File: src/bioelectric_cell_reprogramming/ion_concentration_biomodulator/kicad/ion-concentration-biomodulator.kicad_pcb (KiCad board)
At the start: 4 copper layers, 96 x 72 mm, 69 parts, among them J1 532610671, J10 39-53-2045, J11 Conn_01x14_Pin, J12 Conn_01x14_Pin, J13 39-53-2045, J14 39-53-2045, J15 Conn_ARM_SWD_TagConnect_TC2030, J16 IPL1-104-01-L-D-K, J17 Conn_01x02_Pin, J18 EJ508A, J19 USB_C_Receptacle_USB2.0_14P, J2 532610671, J20 6620XX11122_66200211122, J21 IPL1-102-01-L-S-K, J3 532610671, J4 532610671, J5 S4B-PH-SM4-TB, J6 Conn_01x02_Pin, J7 6620XX11122_66200211122, J8 39-53-2045, J9 IPL1-102-01-L-S-K, Q1 NDT3055L, Q2 NDT3055L, Q4 NDT3055L, Q5 NDT3055L, Q6 NDT3055L, SW1 SW_Push, U1 STM32F410CBTx, U2 LM1084-5.0, U3 LM1084-3.3, U4 USBLC6-2SC6, U5 DRV8873HPWPR

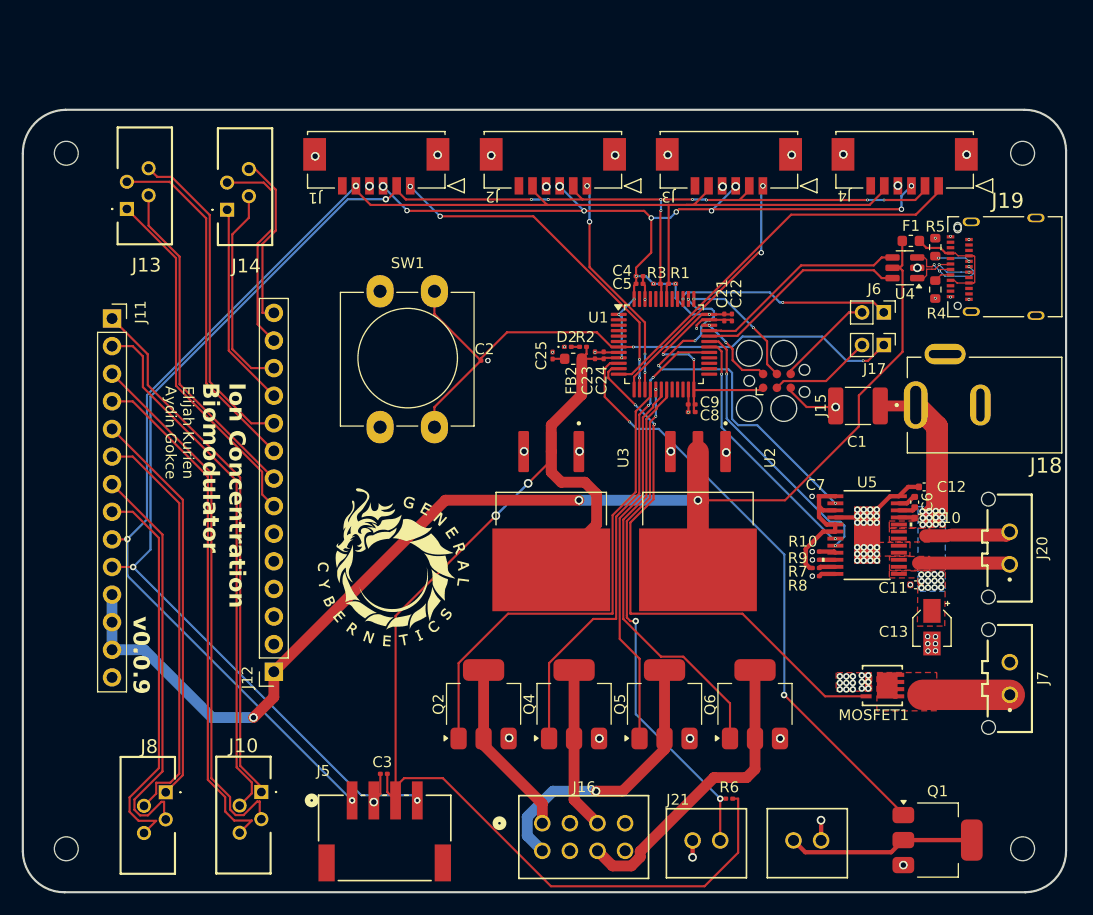
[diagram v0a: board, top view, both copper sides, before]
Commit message: fix: bigger STM32, fix mirrored highdriver pinout
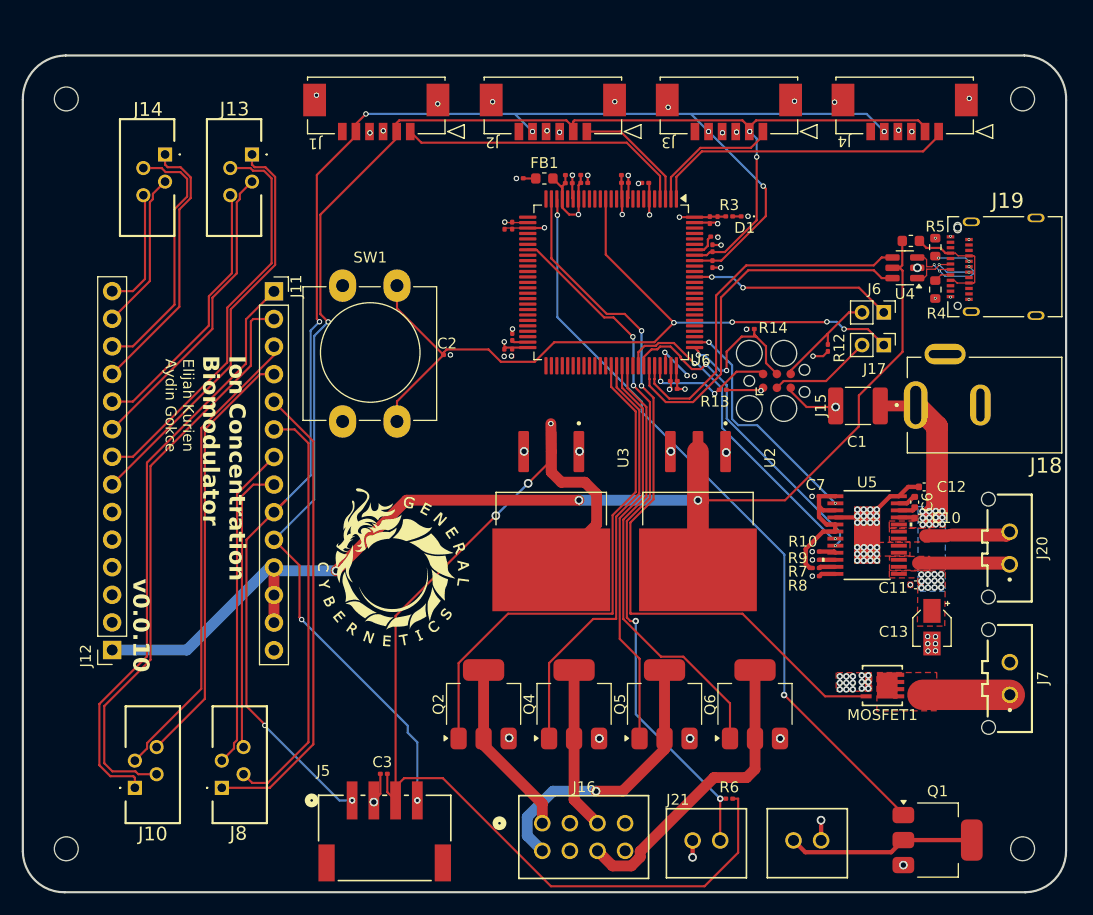
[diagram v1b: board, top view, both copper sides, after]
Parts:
- removed D2: LED, LED_SMD:LED_0201_0603Metric
- removed FB2: 120R, Inductor_SMD:L_0603_1608Metric
- removed U1: STM32F410CBTx, Package_QFP:LQFP-48_7x7mm_P0.5mm
- added C14: 1uF, Capacitor_SMD:C_0201_0603Metric, F.Cu at (154.8, 61.1)
- added C15: 100nF, Capacitor_SMD:C_0201_0603Metric, F.Cu at (154.8, 60.4)
- added C16: 100nF, Capacitor_SMD:C_0201_0603Metric, F.Cu at (149.6, 61.1)
- added C17: 1uF, Capacitor_SMD:C_0201_0603Metric, F.Cu at (145.1, 60.6)
- added C18: 1uF, Capacitor_SMD:C_0201_0603Metric, F.Cu at (149.7, 60.4)
- added C19: 1uF, Capacitor_SMD:C_0201_0603Metric, F.Cu at (151.1, 60.4)
- added C20: 100nF, Capacitor_SMD:C_0201_0603Metric, F.Cu at (151.1, 61.1)
- added C26: 2.2uF, Capacitor_SMD:C_0201_0603Metric, F.Cu at (160.9, 78.8)
- added C27: 100nF, Capacitor_SMD:C_0201_0603Metric, F.Cu at (156.7, 61.1)
- added D1: LED, LED_SMD:LED_0201_0603Metric, F.Cu at (165.8, 64.2)
- added FB1: 120R, Inductor_SMD:L_0603_1608Metric, F.Cu at (147.4, 60.7)
- added R11: 10K, Resistor_SMD:R_0201_0603Metric, F.Cu at (163.0, 66.0)
- added R12: 10K, Resistor_SMD:R_0201_0603Metric, F.Cu at (173.5, 76.3)
- added R13: 10K, Resistor_SMD:R_0201_0603Metric, F.Cu at (163.8, 80.1)
- added R14: 10K, Resistor_SMD:R_0201_0603Metric, F.Cu at (166.4, 74.5)
- added U6: STM32F407VGTx, Package_QFP:LQFP-100_14x14mm_P0.5mm, F.Cu at (153.5, 70.2)
- C23, C4, C8: value 100nF -> 1uF
- C24, C5, C9: value 1uF -> 100nF
- C25: value 1uF -> 2.2uF
- R2: value 220 -> 10K
- R3: value 10K -> 220
- moved C22 22.6 mm to (143.7, 65.0), turned to 90 degrees
- moved C21 21.3 mm to (144.4, 65.0), turned to 90 degrees
- moved J11 15.1 mm to (122.5, 71.1)
- moved J12 15.0 mm to (107.6, 104.1)
- moved R2 15.0 mm to (162.9, 67.1), turned to -90 degrees
- moved J13 12.6 mm to (120.5, 58.5), turned to -90 degrees
- moved J10 11.6 mm to (109.7, 116.7), turned to 90 degrees
- moved C5 9.27 mm to (163.3, 64.5), turned to -90 degrees
- moved C24 9.14 mm to (143.7, 76.7), turned to -90 degrees
- moved R3 9.09 mm to (164.4, 64.2)
- moved C4 8.28 mm to (162.6, 64.5), turned to -90 degrees
- moved J14 7.65 mm to (112.5, 58.5), turned to -90 degrees
- moved C23 7.62 mm to (144.4, 76.7), turned to -90 degrees
- moved J8 5.18 mm to (117.7, 116.7), turned to 90 degrees
- moved H1 5.00 mm to (103.4, 53.4)
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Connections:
- R2 pad 2: Net-(D2-A) -> /I2C_SDA
- R3 pad 2: /I2C_SDA -> Net-(D1-A)
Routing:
- net +3.3V: track 219.2 -> 138.3 mm, vias 21 -> 19
- net /THERM_FEEDBACK: track 46.5 -> 64.7 mm
- net /INCUBATOR_PELT_OUT: track 50.9 -> 68.8 mm
- net /NRST: track 56.9 -> 73.7 mm, vias 2 -> 4
- net /SOLEN_OUT: track 55.2 -> 69.9 mm
- net /D-: track 19.7 -> 34.3 mm
- net /D+: track 19.7 -> 33.6 mm
- net /H_BRIDGE_FAULT: track 34.8 -> 22.0 mm, vias 4 -> 2
- net /IRQn2: track 23.8 -> 12.0 mm, vias 2 -> 0
- net /IRQn4: track 20.9 -> 11.0 mm, vias 4 -> 0
- net /31-: track 36.0 -> 26.3 mm
- net /IRQn1: track 36.9 -> 27.7 mm
- net /31+: track 38.1 -> 29.9 mm
- net /41-: track 47.6 -> 39.5 mm
- net /I2C_SDA: track 146.5 -> 138.7 mm, vias 11 -> 5
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- added copper zone on In2.Cu, net +3.3V
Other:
- board size 96 x 72 mm -> 96 x 77 mm
- board text added: "v0.0.10"
- board text removed: "v0.0.9"

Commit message: fix: new co2 sensor
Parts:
- added J22: IPL1-104-01-X-S-K, IPL1_104_01_L_S_K:SAMTEC_IPL1-104-01-X-S-K, F.Cu at (175.3, 61.7)
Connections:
- U6 pad 86: unconnected-(U6-PD5-Pad86) -> /USART2_TX
- U6 pad 87: unconnected-(U6-PD6-Pad87) -> /USART2_RX
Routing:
- net /USART2_RX: track 0.00 -> 19.2 mm
- net /USART2_TX: track 0.00 -> 14.8 mm
- net +3.3V: track 138.3 -> 143.9 mm, vias 19 -> 20

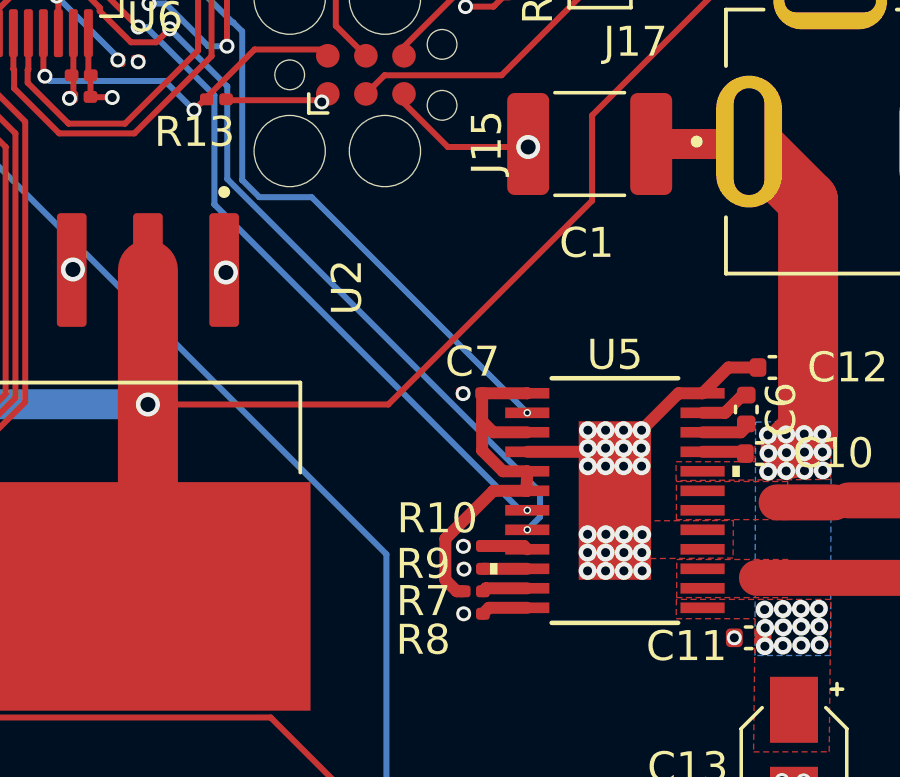
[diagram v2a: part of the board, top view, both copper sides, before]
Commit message: fix: DRV8873 nSLEEP and nFAULT pull-ups
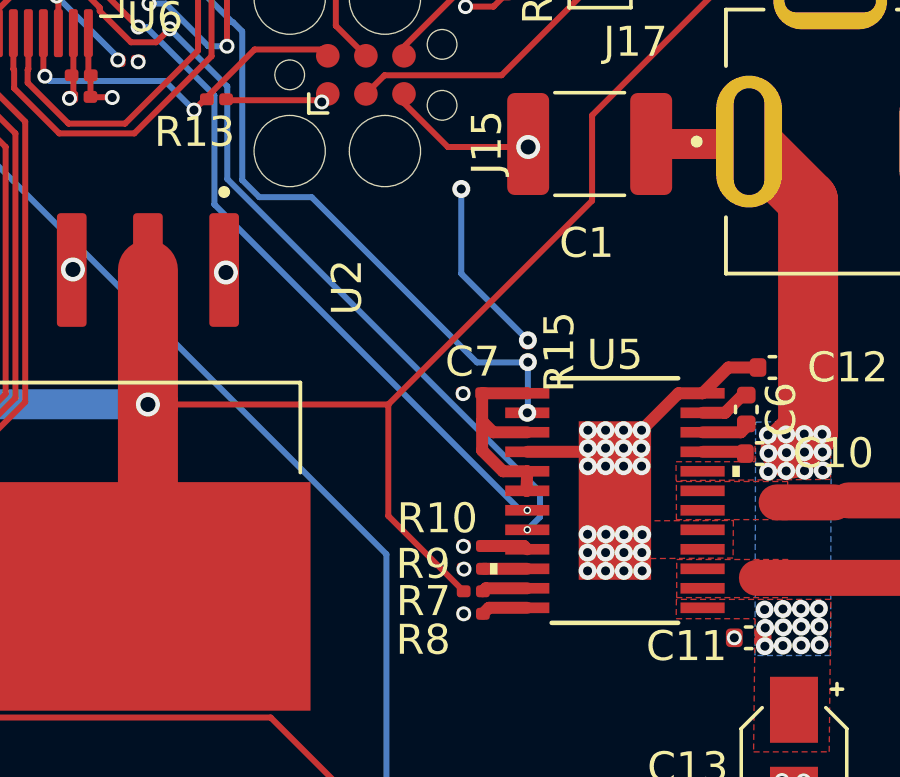
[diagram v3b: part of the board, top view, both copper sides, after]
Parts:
- added R15: 10K, Resistor_SMD:R_0201_0603Metric, F.Cu at (174.2, 88.5)
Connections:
- R7 pad 1: /peltier_coolers/DVDD -> +5V
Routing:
- net +5V: track 113.1 -> 120.3 mm
- net +3.3V: track 143.9 -> 149.8 mm, vias 20 -> 22
- net /peltier_coolers/DVDD: track 13.1 -> 7.54 mm
- net /H_BRIDGE_FAULT: track 22.0 -> 23.0 mm, vias 2 -> 3

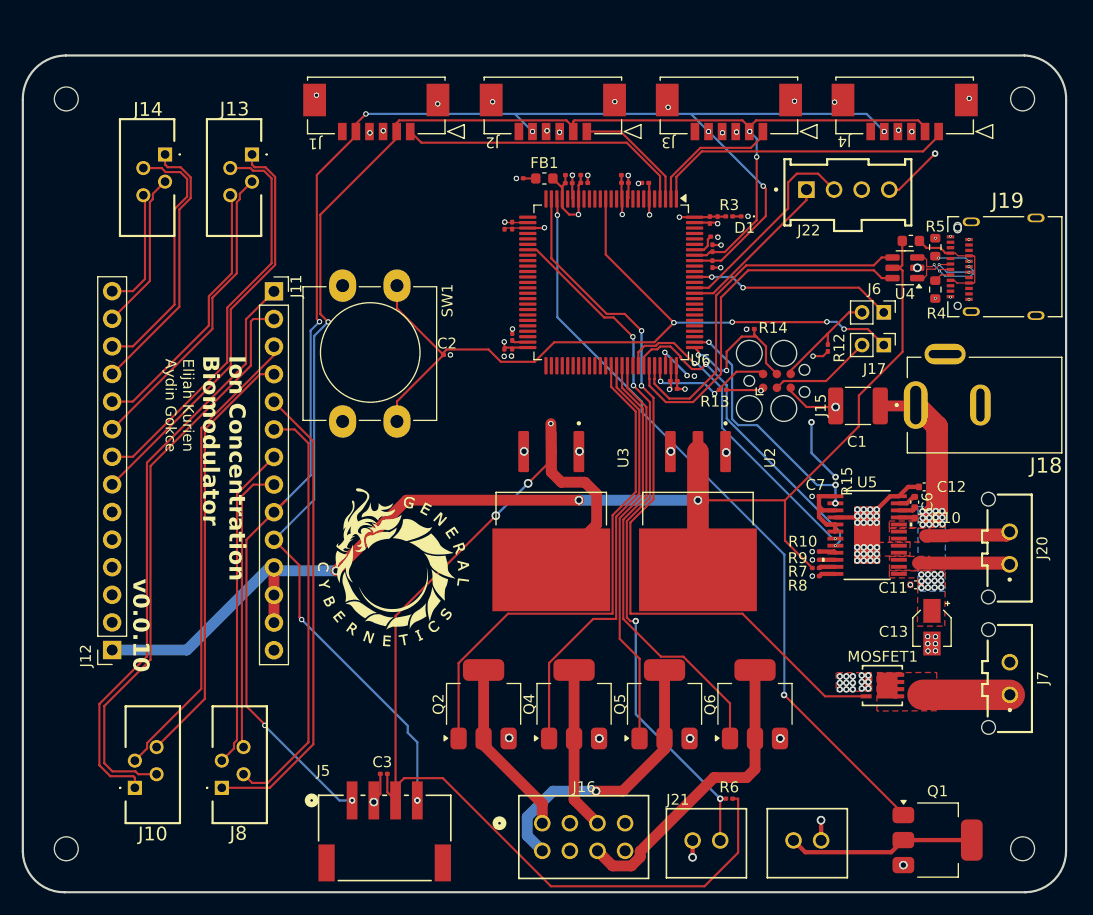
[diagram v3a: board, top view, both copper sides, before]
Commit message: fix: HSE for USB FS
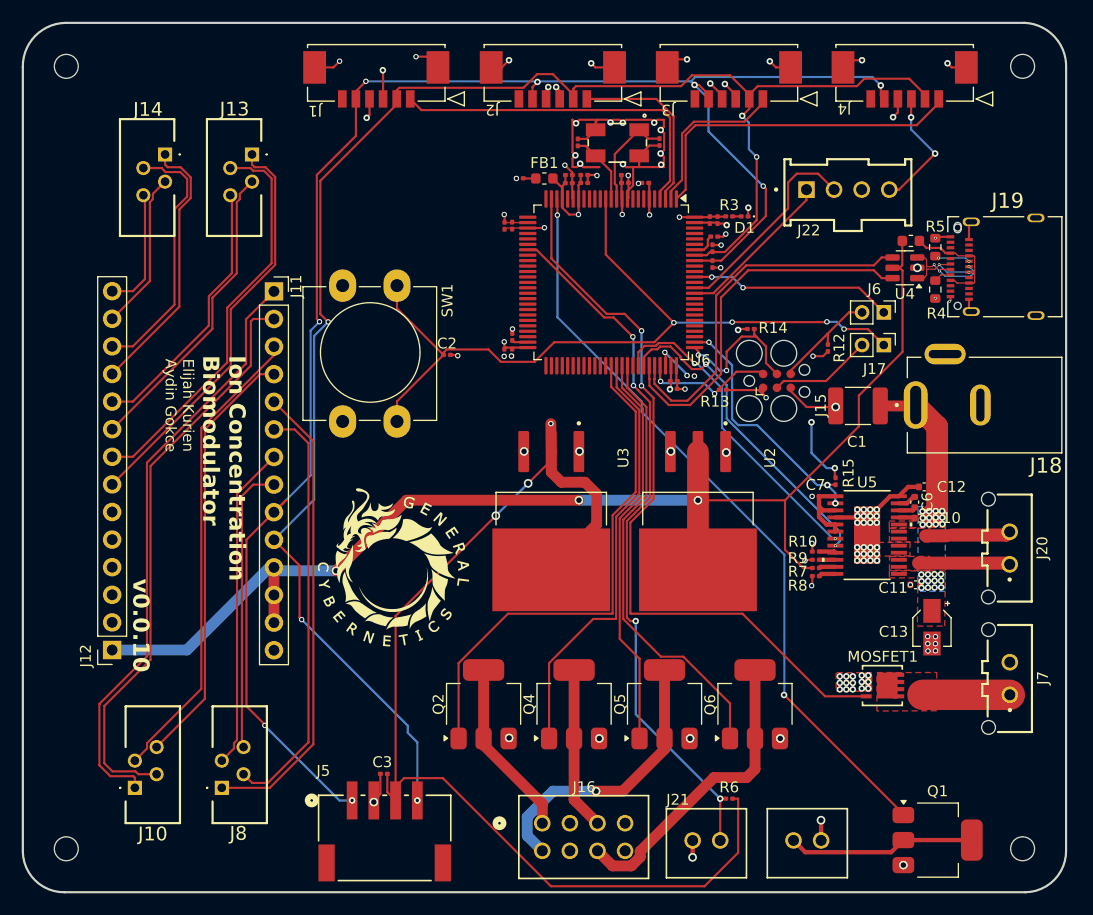
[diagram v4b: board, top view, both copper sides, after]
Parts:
- added C28: 33pF, Capacitor_SMD:C_0201_0603Metric, F.Cu at (150.5, 57.4)
- added C29: 33pF, Capacitor_SMD:C_0201_0603Metric, F.Cu at (158.0, 57.3)
- added X1: ABM3B-8.000MHZ-B2-T, ABM3B_8_000MHZ_B2_T:ABM3B_ABR, F.Cu at (154.1, 57.4)
- moved H1 3.00 mm to (103.4, 50.4)
- moved H2 3.00 mm to (191.4, 50.4)
- moved J1 3.00 mm to (135.1, 53.4)
- moved J2 3.00 mm to (151.3, 53.4)
- moved J3 3.00 mm to (167.5, 53.3)
- moved J4 3.00 mm to (183.7, 53.4)
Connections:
- U6 pad 12: unconnected-(U6-PH0-Pad12) -> /stm32/OSC_IN
- U6 pad 13: unconnected-(U6-PH1-Pad13) -> /stm32/OSC_OUT
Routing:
- net GND: track 28.2 -> 102.2 mm, vias 94 -> 101
- net +3.3V: track 149.8 -> 164.3 mm
- net /I2C_SDA: track 138.7 -> 148.5 mm
- net /stm32/OSC_IN: track 0.00 -> 9.67 mm
- net /I2C_SCK: track 145.7 -> 154.6 mm
- net /stm32/OSC_OUT: track 0.00 -> 6.58 mm
- net /IRQn3: track 26.8 -> 32.5 mm
- net /IRQn4: track 11.0 -> 16.6 mm
- net /IRQn1: track 27.7 -> 30.7 mm
- net /IRQn2: track 12.0 -> 15.0 mm
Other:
- board size 96 x 77 mm -> 96 x 80 mm

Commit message: feat: oscillator plus mfg files
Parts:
- removed F1: 500mA, Fuse:Fuse_0603_1608Metric
- removed J19: USB_C_Receptacle_USB2.0_14P, 12401610E4_2A.pretty:AMPHENOL_12401610E4_2A
- removed U4: USBLC6-2SC6, Package_TO_SOT_SMD:SOT-23-6
- added USBC1: ~, USB-C-SMD_MC-311D:USB-C-SMD_MC-311D, F.Cu at (190.3, 69.4)
- moved R5 5.45 mm to (186.3, 71.6), turned to -90 degrees
- moved R4 4.89 mm to (186.2, 66.9), turned to 90 degrees
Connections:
- R4 pad 1: /CC1 -> /CC2
- R5 pad 1: /CC2 -> /CC1
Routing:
- net /VBUS: track 10.4 -> 0.00 mm
- net /D+_in: track 8.48 -> 0.00 mm, vias 3 -> 0
- net /D+: track 33.8 -> 40.4 mm, vias 0 -> 2
- net /D-_in: track 6.12 -> 0.00 mm, vias 2 -> 0
- net /D-: track 34.5 -> 40.2 mm, vias 0 -> 2
- net +3.3V: track 164.3 -> 166.9 mm
- net /H_BRIDGE_IN2: track 30.0 -> 32.4 mm
- net GND: track 102.2 -> 104.4 mm, vias 101 -> 97
- net +5V: track 120.8 -> 119.3 mm
- net /NRST: track 73.7 -> 72.2 mm
- net /CC2: track 2.92 -> 1.77 mm, vias 2 -> 0
- net /INCUBATOR_PELT_OUT: track 68.8 -> 67.8 mm
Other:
- board text added: "v0.0.11"
- board text removed: "v0.0.10"
